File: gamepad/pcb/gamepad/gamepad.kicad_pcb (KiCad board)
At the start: 2 copper layers, 100 x 100 mm, 9 parts, among them U1 Pico

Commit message: upt(gamepad): working on pcb
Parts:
- moved U1 31.2 mm to (74.3, 89.3), turned to 180 degrees
- renumbered ButtonConnector1 to dPad_east1, ButtonConnector6 to dPad_north1, ButtonConnector2 to dPad_south1, ButtonConnector3 to dPad_west1, JoystickConnector2 to joystick_left1, JoystickConnector1 to joystick_right1, ButtonConnector5 to operators_minus1, ButtonConnector4 to operators_plus1
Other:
- board size 100 x 100 mm -> 67.8 x 67.8 mm

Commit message: upt(gamepad): working on pcb
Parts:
- moved dPad_north1 130.3 mm to (115.5, 103.5)
- moved dPad_south1 126.5 mm to (114.5, 88.0)
- moved joystick_left1 123.5 mm to (102.0, 117.5)
- moved joystick_right1 112.9 mm to (98.5, 107.0)
- moved operators_minus1 112.9 mm to (105.0, 96.5)
- moved dPad_west1 108.2 mm to (104.5, 82.0)
- moved dPad_east1 83.8 mm to (116.0, 75.0)
- moved operators_plus1 73.4 mm to (105.5, 67.0)
- moved U1 3.96 mm to (78.1, 90.4), turned to 0 degrees

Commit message: upt: gamepad pcb
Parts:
- added U2: MCU-MCP3008-I_P_DIP16-7.62MM_, MCU-MCP3008:DIP16-2.54-19.2X7.62MM, F.Cu at (108.7, 70.2)
- moved dPad_south1 18.6 mm to (98.5, 97.5)
- moved dPad_east1 18.4 mm to (107.0, 91.0)
- moved operators_plus1 17.6 mm to (99.5, 83.5)
- moved dPad_west1 17.0 mm to (116.5, 94.0)
- moved operators_minus1 6.99 mm to (108.5, 102.5)
- moved joystick_left1 6.52 mm to (108.5, 118.0)
- moved dPad_north1 6.09 mm to (118.0, 109.0)
- moved joystick_right1 4.03 mm to (98.0, 111.0)
- moved U1 2.00 mm to (76.1, 90.4)

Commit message: upt: start wiring schematic
just gotta make sure it works on a breadboard before ordering a pcb
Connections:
- U1 pad 1: unconnected-(U1-GPIO0-Pad1) -> Net-(U1-GPIO0)
- U1 pad 2: unconnected-(U1-GPIO1-Pad2) -> Net-(U1-GPIO1)
- U1 pad 21: unconnected-(U1-GPIO16-Pad21) -> Net-(U1-GPIO16)
- U1 pad 22: unconnected-(U1-GPIO17-Pad22) -> Net-(U1-GPIO17)
- U1 pad 23: unconnected-(U1-GND-Pad23) -> GND
- U1 pad 24: unconnected-(U1-GPIO18-Pad24) -> Net-(U1-GPIO18)
- U1 pad 25: unconnected-(U1-GPIO19-Pad25) -> Net-(U1-GPIO19)
- U1 pad 36: unconnected-(U1-3V3-Pad36) -> +3V3
- U1 pad 4: unconnected-(U1-GPIO2-Pad4) -> Net-(U1-GPIO2)
- U1 pad 5: unconnected-(U1-GPIO3-Pad5) -> Net-(U1-GPIO3)
- U1 pad 6: unconnected-(U1-GPIO4-Pad6) -> Net-(U1-GPIO4)
- U1 pad 7: unconnected-(U1-GPIO5-Pad7) -> Net-(U1-GPIO5)
- U2 pad 1: unconnected-(U2-CH0-Pad1) -> Net-(U2-CH0)
- U2 pad 10: unconnected-(U2-SHDN/~{CS}-Pad10) -> Net-(U1-GPIO17)
- U2 pad 11: unconnected-(U2-DIN-Pad11) -> Net-(U1-GPIO19)
- U2 pad 12: unconnected-(U2-DOUT-Pad12) -> Net-(U1-GPIO16)
- U2 pad 13: unconnected-(U2-CLK-Pad13) -> Net-(U1-GPIO18)
- U2 pad 14: unconnected-(U2-AGND-Pad14) -> GND
- U2 pad 15: unconnected-(U2-VREF-Pad15) -> +3V3
- U2 pad 16: unconnected-(U2-VDD-Pad16) -> +3V3
- U2 pad 2: unconnected-(U2-CH1-Pad2) -> Net-(U2-CH1)
- U2 pad 3: unconnected-(U2-CH2-Pad3) -> Net-(U2-CH2)
- U2 pad 4: unconnected-(U2-CH3-Pad4) -> Net-(U2-CH3)
- U2 pad 9: unconnected-(U2-DGND-Pad9) -> GND
- dPad_east1 pad 1: unconnected-(dPad_east1-Pin_1-Pad1) -> Net-(U1-GPIO1)
- dPad_east1 pad 2: unconnected-(dPad_east1-Pin_2-Pad2) -> GND
- dPad_north1 pad 1: unconnected-(dPad_north1-Pin_1-Pad1) -> Net-(U1-GPIO0)
- dPad_north1 pad 2: unconnected-(dPad_north1-Pin_2-Pad2) -> GND
- dPad_south1 pad 1: unconnected-(dPad_south1-Pin_1-Pad1) -> Net-(U1-GPIO2)
- dPad_south1 pad 2: unconnected-(dPad_south1-Pin_2-Pad2) -> GND
- dPad_west1 pad 1: unconnected-(dPad_west1-Pin_1-Pad1) -> Net-(U1-GPIO3)
- dPad_west1 pad 2: unconnected-(dPad_west1-Pin_2-Pad2) -> GND
- joystick_left1 pad 2: unconnected-(joystick_left1-Pin_2-Pad2) -> Net-(U2-CH0)
- joystick_left1 pad 3: unconnected-(joystick_left1-Pin_3-Pad3) -> Net-(U2-CH1)
- joystick_left1 pad 5: unconnected-(joystick_left1-Pin_5-Pad5) -> GND
- joystick_right1 pad 2: unconnected-(joystick_right1-Pin_2-Pad2) -> Net-(U2-CH2)
- joystick_right1 pad 3: unconnected-(joystick_right1-Pin_3-Pad3) -> Net-(U2-CH3)
- joystick_right1 pad 5: unconnected-(joystick_right1-Pin_5-Pad5) -> GND
- operators_minus1 pad 1: unconnected-(operators_minus1-Pin_1-Pad1) -> Net-(U1-GPIO5)
- operators_minus1 pad 2: unconnected-(operators_minus1-Pin_2-Pad2) -> GND
- operators_plus1 pad 1: unconnected-(operators_plus1-Pin_1-Pad1) -> Net-(U1-GPIO4)
- operators_plus1 pad 2: unconnected-(operators_plus1-Pin_2-Pad2) -> GND

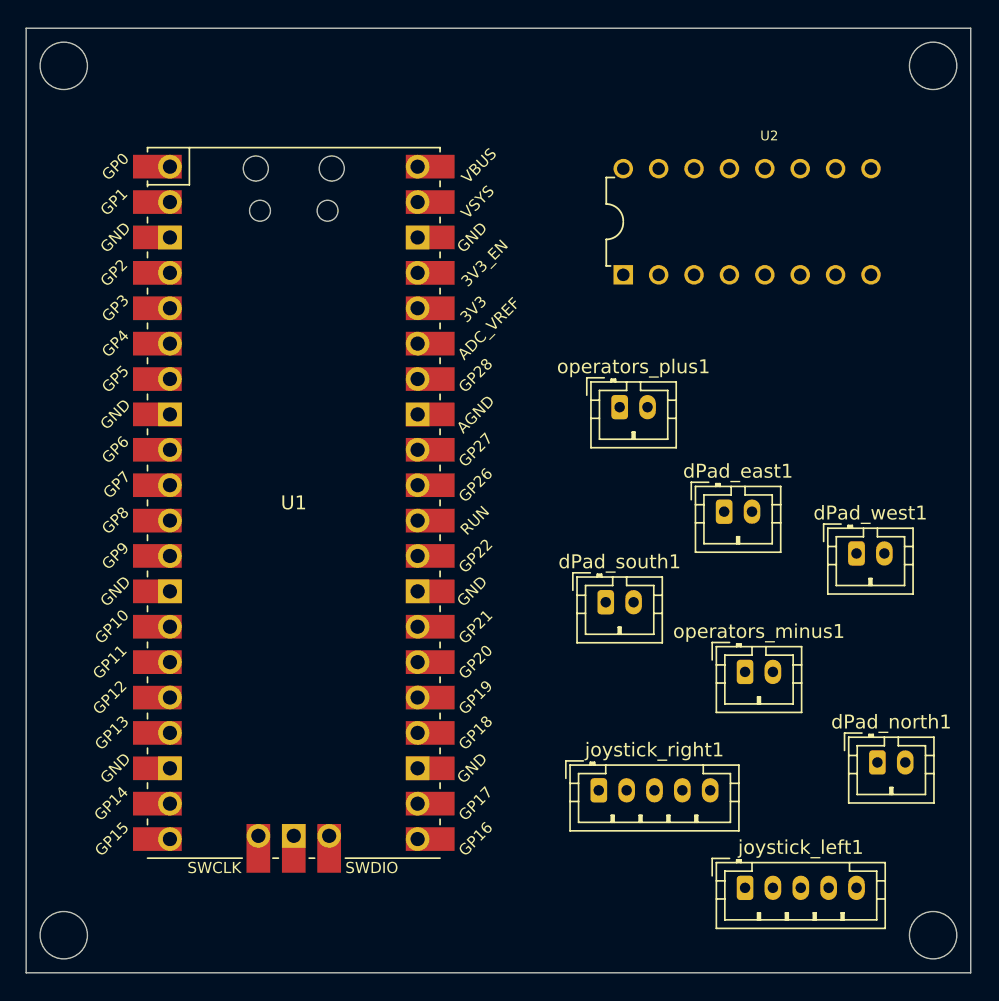
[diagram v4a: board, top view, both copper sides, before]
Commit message: upt: some stuff for the pcb
- routed the traces
- cleaned up the wiring for the schematic
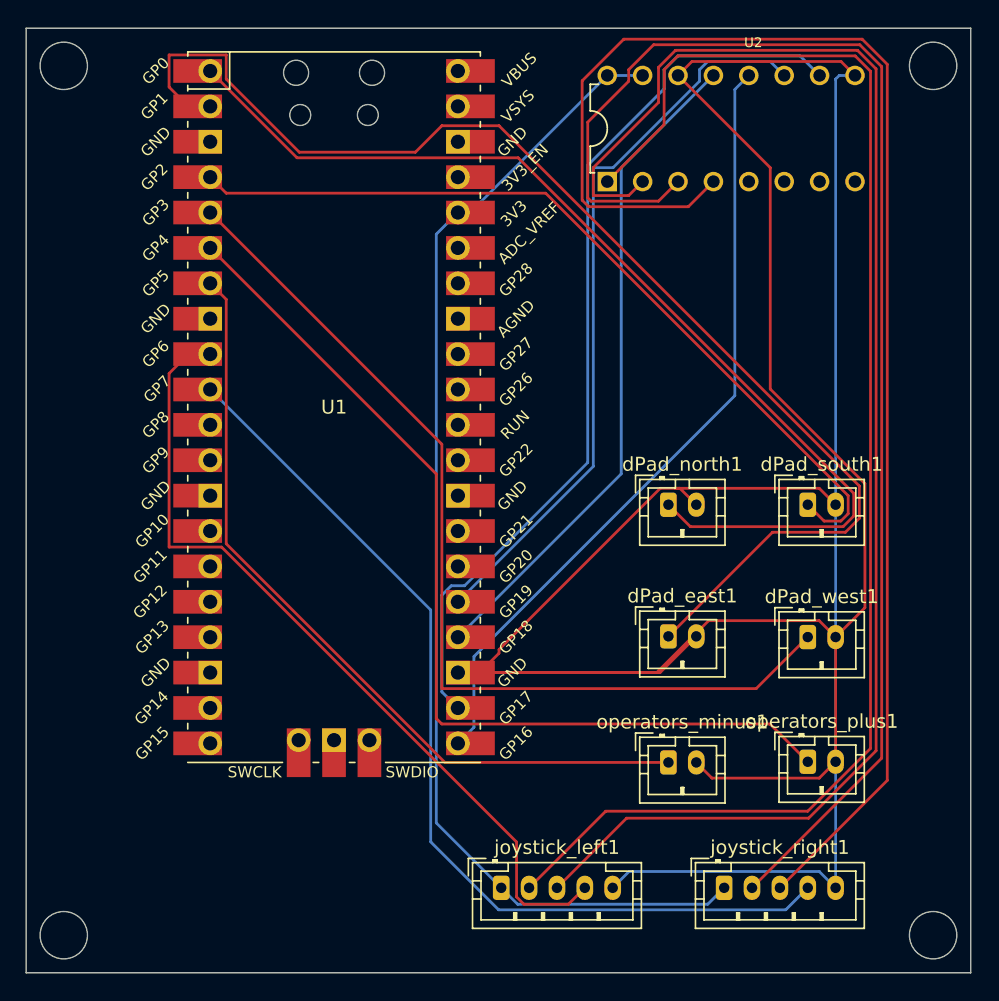
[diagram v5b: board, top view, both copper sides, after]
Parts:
- U2: value MCU-MCP3008-I_P_DIP16-7.62MM_ -> ADC
- moved operators_plus1 28.8 mm to (113.0, 109.0)
- moved dPad_north1 23.8 mm to (103.0, 90.5)
- moved joystick_left1 17.5 mm to (91.0, 118.0)
- moved dPad_south1 16.1 mm to (113.0, 90.5)
- moved joystick_right1 11.4 mm to (107.0, 118.0)
- moved dPad_east1 9.80 mm to (103.0, 100.0)
- moved operators_minus1 8.51 mm to (103.0, 109.0)
- moved U1 7.45 mm to (79.0, 83.5)
- moved dPad_west1 6.95 mm to (113.0, 100.0)
- moved U2 6.79 mm to (107.5, 63.5)
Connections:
- U1 pad 10: unconnected-(U1-GPIO7-Pad10) -> Net-(U1-GPIO7)
- U1 pad 9: unconnected-(U1-GPIO6-Pad9) -> Net-(U1-GPIO6)
- joystick_left1 pad 1: unconnected-(joystick_left1-Pin_1-Pad1) -> +3V3
- joystick_left1 pad 4: unconnected-(joystick_left1-Pin_4-Pad4) -> Net-(U1-GPIO6)
- joystick_right1 pad 1: unconnected-(joystick_right1-Pin_1-Pad1) -> +3V3
- joystick_right1 pad 4: unconnected-(joystick_right1-Pin_4-Pad4) -> Net-(U1-GPIO7)
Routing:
- net GND: track 0.00 -> 239.2 mm
- net Net-(U2-CH1): track 0.00 -> 107.7 mm
- net Net-(U2-CH3): track 0.00 -> 105.1 mm
- net Net-(U2-CH0): track 0.00 -> 102.7 mm
- net Net-(U2-CH2): track 0.00 -> 99.9 mm
- net Net-(U1-GPIO1): track 0.00 -> 90.3 mm
- net +3V3: track 0.00 -> 85.4 mm
- net Net-(U1-GPIO0): track 0.00 -> 76.2 mm
- net Net-(U1-GPIO3): track 0.00 -> 68.9 mm
- net Net-(U1-GPIO7): track 0.00 -> 68.8 mm
- net Net-(U1-GPIO4): track 0.00 -> 68.4 mm
- net Net-(U1-GPIO17): track 0.00 -> 65.6 mm
- net Net-(U1-GPIO2): track 0.00 -> 60.2 mm
- net Net-(U1-GPIO6): track 0.00 -> 59.2 mm
- net Net-(U1-GPIO5): track 0.00 -> 57.4 mm
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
